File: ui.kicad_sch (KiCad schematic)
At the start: 7 parts, among them J17 Conn_01x14_MountingPin, J18 Conn_01x14_MountingPin, Q11 IRLML2502

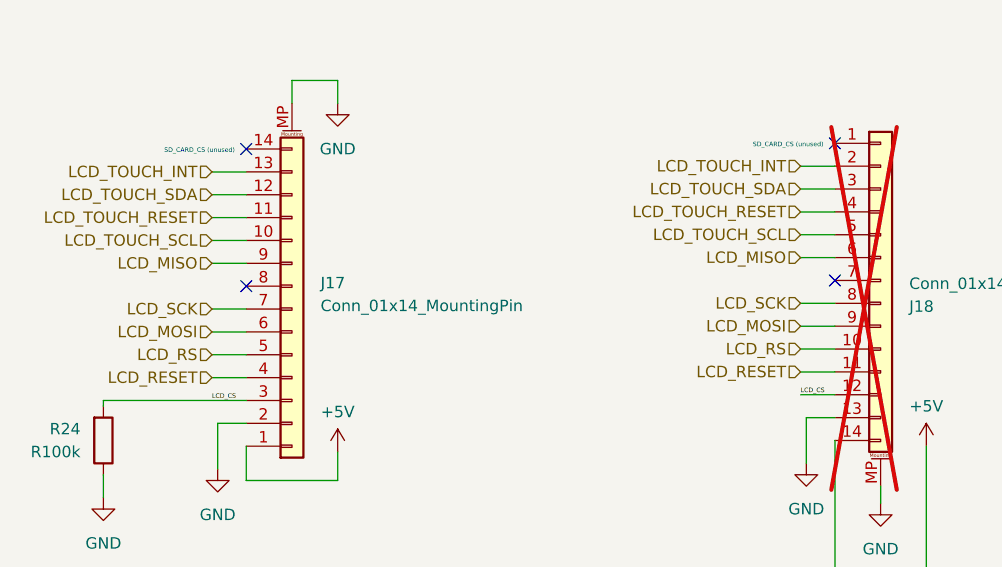
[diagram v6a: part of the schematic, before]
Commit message: Redesign power rails to use barrel jack 12V input
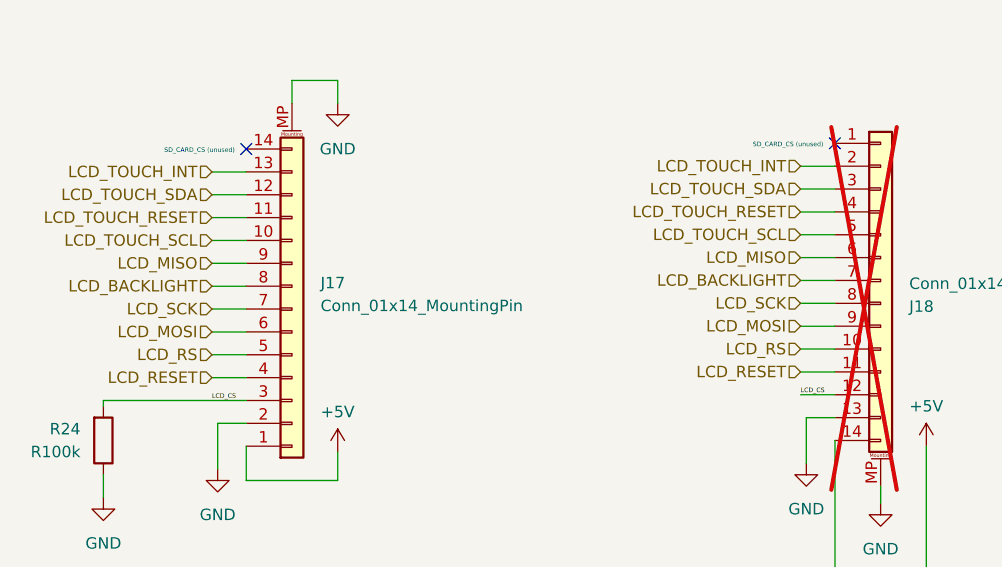
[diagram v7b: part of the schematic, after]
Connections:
- net LCD_BACKLIGHT: now reaches J17.8 (Pin_8)
- net LCD_BACKLIGHT: now also J18.7 (Pin_7)
- no-connect marks 4 -> 2
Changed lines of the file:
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@@
   (junction (at 213.995 90.805) (diameter 0) (color 0 0 0 0)
   )
-  (no_connect (at 128.27 88.9))
   (no_connect (at 62.865 74.295))
-  (no_connect (at 62.865 89.535))
   (no_connect (at 128.27 73.66))
   (wire (pts (xy 67.945 69.215) (xy 67.945 66.675))
@@
     (stroke (width 0) (type default))
   )
+  (wire (pts (xy 124.46 88.9) (xy 128.27 88.9))
+    (stroke (width 0) (type default))
+  )
   (wire (pts (xy 230.505 81.28) (xy 226.695 81.28))
     (stroke (width 0) (type default))
@@
   )
   (wire (pts (xy 59.055 86.995) (xy 62.865 86.995))
+    (stroke (width 0) (type default))
+  )
+  (wire (pts (xy 59.055 89.535) (xy 62.865 89.535))
     (stroke (width 0) (type default))
   )
@@
     (effects (font (size 0.504 0.504)) (justify left bottom))
   )
+  (hierarchical_label "LCD_BACKLIGHT" (shape input) (at 59.055 89.535 180) (fields_autoplaced)
+    (effects (font (size 1.27 1.27)) (justify right))
+  )
   (hierarchical_label "LCD_RESET" (shape input) (at 124.46 99.06 180) (fields_autoplaced)
     (effects (font (size 1.27 1.27)) (justify right))
@@
     (effects (font (size 1.27 1.27)) (justify right))
   )
+  (hierarchical_label "LCD_BACKLIGHT" (shape input) (at 124.46 88.9 180) (fields_autoplaced)
+    (effects (font (size 1.27 1.27)) (justify right))
+  )

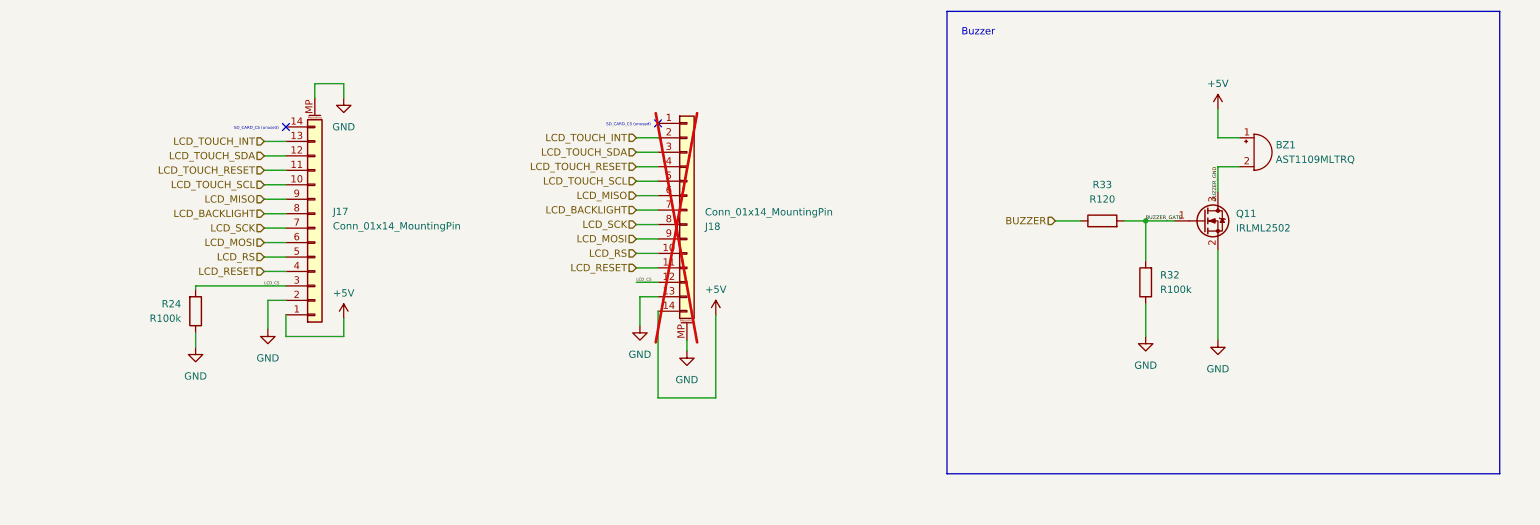
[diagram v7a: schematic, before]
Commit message: Reannotate geographically by layout
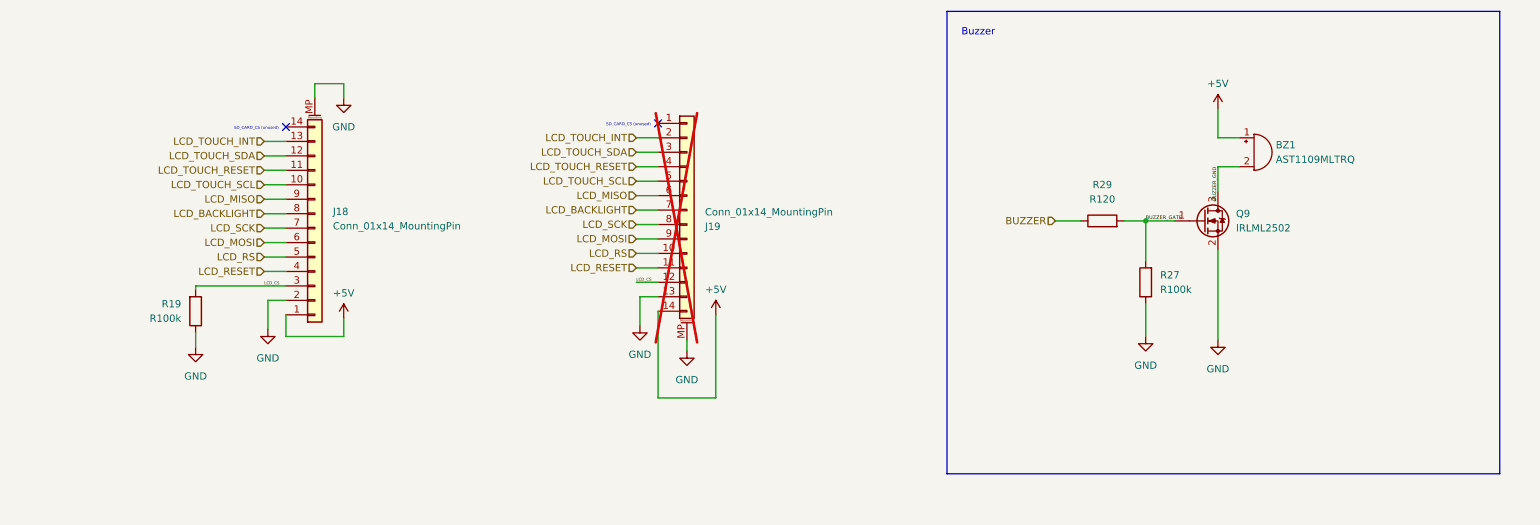
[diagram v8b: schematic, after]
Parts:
- renumbered J17 to J18, J18 to J19, Q11 to Q9, R24 to R19, R32 to R27, R33 to R29
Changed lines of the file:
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@@
   (symbol (lib_id "Device:R") (at 213.995 101.6 180) (unit 1)
     (in_bom yes) (on_board yes) (dnp no) (fields_autoplaced)
-    (property "Reference" "R32" (at 216.535 100.33 0)
+    (property "Reference" "R27" (at 216.535 100.33 0)
       (effects (font (size 1.27 1.27)) (justify right))
     )
@@
       (project "mainboard"
         (path "/613f8c39-c37c-4981-8911-5138d36a7959/e16aa466-f341-4735-929a-c85f813defce"
-          (reference "R32") (unit 1)
+          (reference "R27") (unit 1)
         )
       )
@@
   (symbol (lib_id "Device:Q_NMOS_GSD") (at 224.155 90.805 0) (unit 1)
     (in_bom yes) (on_board yes) (dnp no) (fields_autoplaced)
-    (property "Reference" "Q11" (at 229.87 89.535 0)
+    (property "Reference" "Q9" (at 229.87 89.535 0)
       (effects (font (size 1.27 1.27)) (justify left))
     )
@@
       (project "mainboard"
         (path "/613f8c39-c37c-4981-8911-5138d36a7959/e16aa466-f341-4735-929a-c85f813defce"
-          (reference "Q11") (unit 1)
+          (reference "Q9") (unit 1)
         )
       )
@@
   (symbol (lib_id "Device:R") (at 46.99 106.68 0) (mirror x) (unit 1)
     (in_bom yes) (on_board yes) (dnp no)
-    (property "Reference" "R24" (at 44.45 105.41 0)
+    (property "Reference" "R19" (at 44.45 105.41 0)
       (effects (font (size 1.27 1.27)) (justify right))
     )
@@
       (project "mainboard"
         (path "/613f8c39-c37c-4981-8911-5138d36a7959/e16aa466-f341-4735-929a-c85f813defce"
-          (reference "R24") (unit 1)
+          (reference "R19") (unit 1)
         )
       )
@@
   (symbol (lib_id "Device:R") (at 206.375 90.805 90) (unit 1)
     (in_bom yes) (on_board yes) (dnp no) (fields_autoplaced)
-    (property "Reference" "R33" (at 206.375 84.455 90)
+    (property "Reference" "R29" (at 206.375 84.455 90)
       (effects (font (size 1.27 1.27)))
     )
@@
       (project "mainboard"
         (path "/613f8c39-c37c-4981-8911-5138d36a7959/e16aa466-f341-4735-929a-c85f813defce"
-          (reference "R33") (unit 1)
+          (reference "R29") (unit 1)
         )
       )
@@
   (symbol (lib_id "Connector_Generic_MountingPin:Conn_01x14_MountingPin") (at 67.945 92.075 0) (mirror x) (unit 1)
     (in_bom yes) (on_board yes) (dnp no) (fields_autoplaced)
-    (property "Reference" "J17" (at 71.12 89.1794 0)
+    (property "Reference" "J18" (at 71.12 89.1794 0)
       (effects (font (size 1.27 1.27)) (justify left))
     )
@@
       (project "mainboard"
         (path "/613f8c39-c37c-4981-8911-5138d36a7959/e16aa466-f341-4735-929a-c85f813defce"
-          (reference "J17") (unit 1)
+          (reference "J18") (unit 1)
         )
       )
@@
   (symbol (lib_id "Connector_Generic_MountingPin:Conn_01x14_MountingPin") (at 133.35 88.9 0) (unit 1)
     (in_bom yes) (on_board yes) (dnp yes)
-    (property "Reference" "J18" (at 136.525 91.7956 0)
+    (property "Reference" "J19" (at 136.525 91.7956 0)
       (effects (font (size 1.27 1.27)) (justify left))
     )
@@
       (project "mainboard"
         (path "/613f8c39-c37c-4981-8911-5138d36a7959/e16aa466-f341-4735-929a-c85f813defce"
-          (reference "J18") (unit 1)
-        )
-      )
+          (reference "J19") (unit 1)
+        )
+      )
